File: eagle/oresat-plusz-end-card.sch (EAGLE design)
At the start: 13 parts, among them J1 J-SAMTEC-TFM-110-X1-XXX-D-RA, J2 U.FL

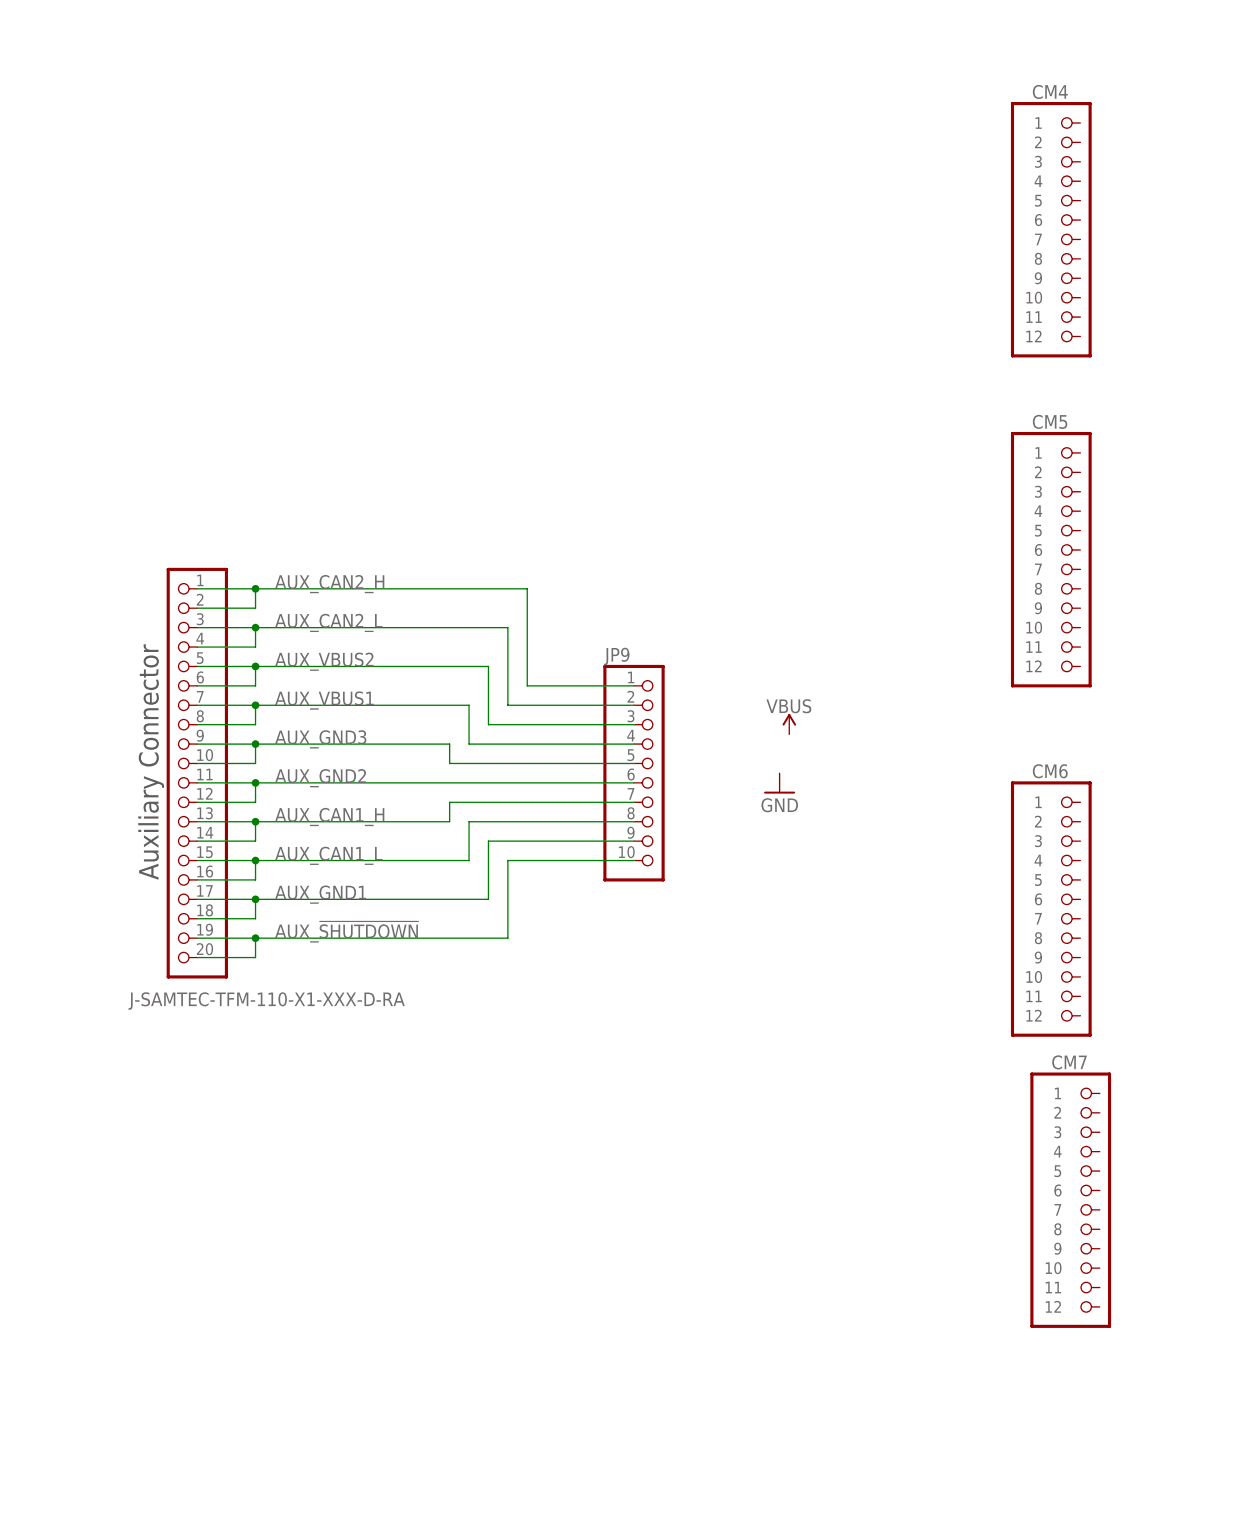
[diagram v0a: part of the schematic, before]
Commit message: Created library and placed solar connectors based on structure updates from yesterday.
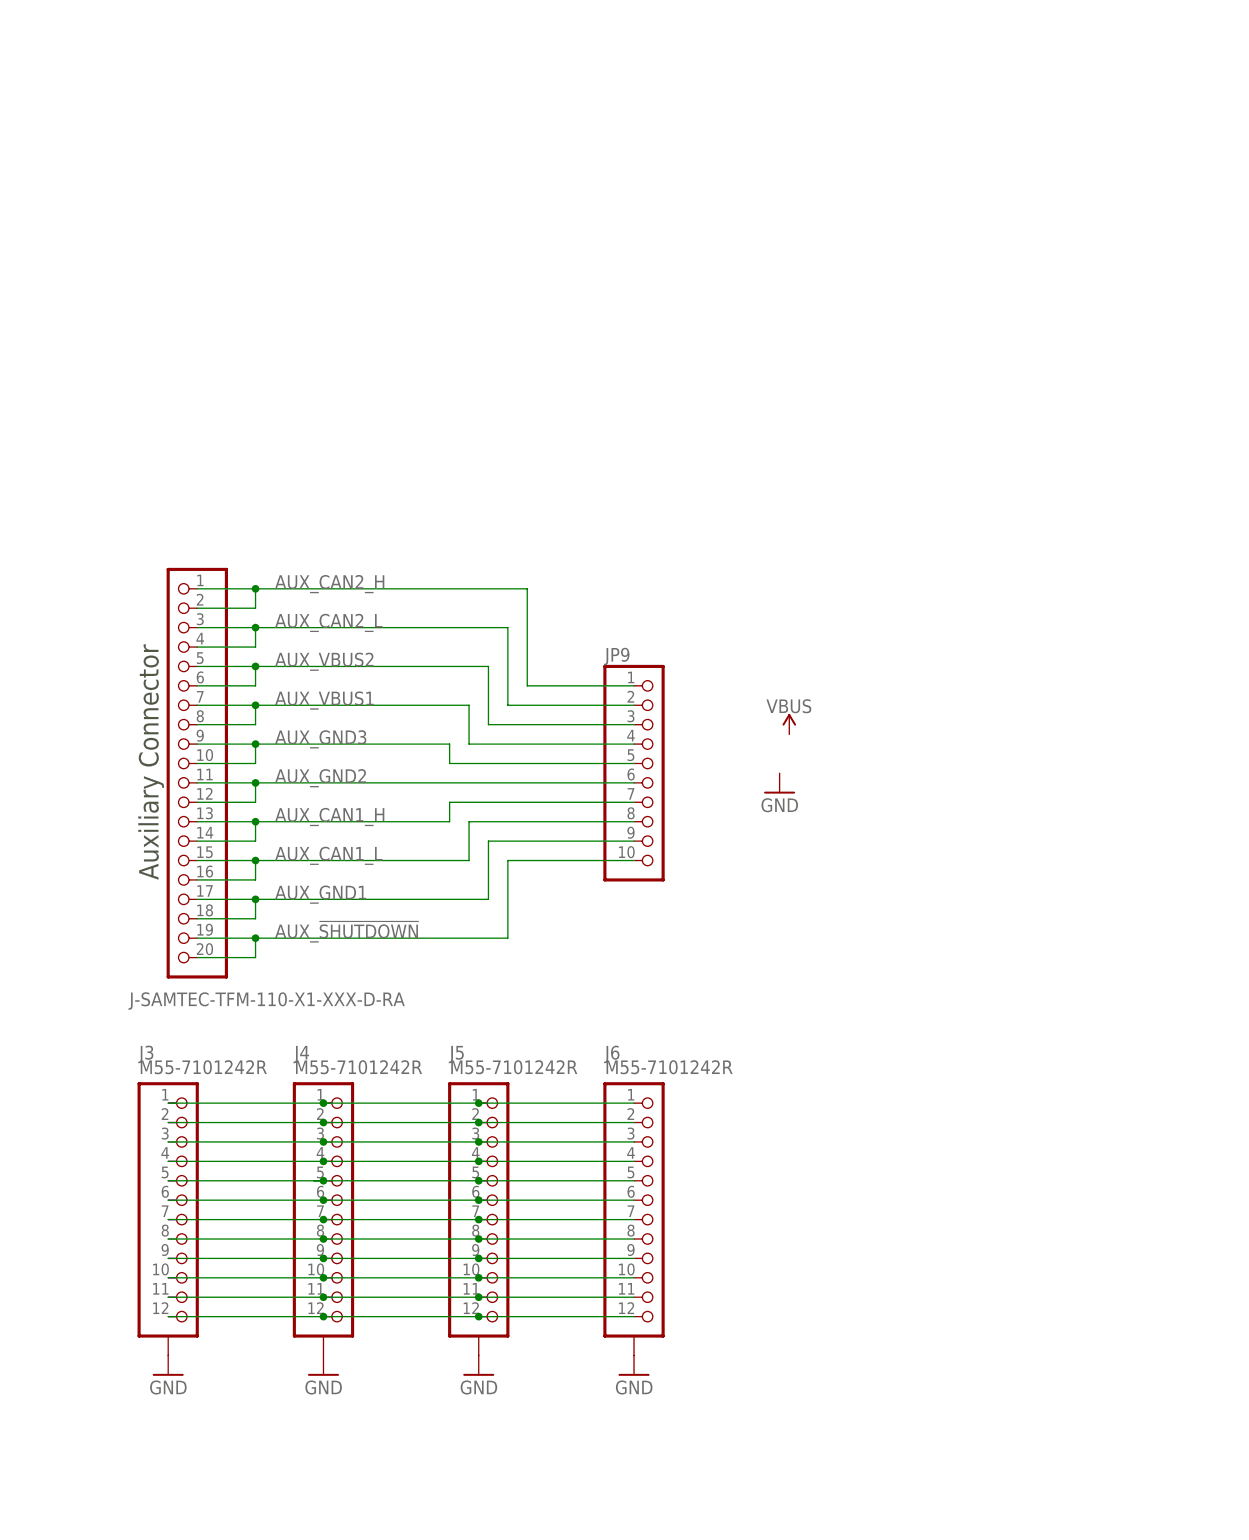
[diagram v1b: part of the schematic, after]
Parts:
- removed CM4, CM5, CM6, CM7: ORESAT-SOLARPANEL-CARD-12PIN, oresat-connectors:ORESAT-SOLARPANEL-CARD-12PIN
- added J3, J4, J5, J6: M55-7101242R, J-Harwin-M55-7101242:M55-7101242R
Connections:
- new net N$1: J3.1, J4.1, J5.1, J6.1
- new net N$10: J3.10, J4.10, J5.10, J6.10
- new net N$11: J3.11, J4.11, J5.11, J6.11
- new net N$12: J3.12, J4.12, J5.12, J6.12
- new net N$2: J3.2, J4.2, J5.2, J6.2
- new net N$3: J3.3, J4.3, J5.3, J6.3
- new net N$4: J3.4, J4.4, J5.4, J6.4
- new net N$5: J3.5, J4.5, J5.5, J6.5
- new net N$6: J3.6, J4.6, J5.6, J6.6
- new net N$7: J3.7, J4.7, J5.7, J6.7
- new net N$8: J3.8, J4.8, J5.8, J6.8
- new net N$9: J3.9, J4.9, J5.9, J6.9
- net GND: now also J3.SHIELD, J4.SHIELD, J5.SHIELD, J6.SHIELD

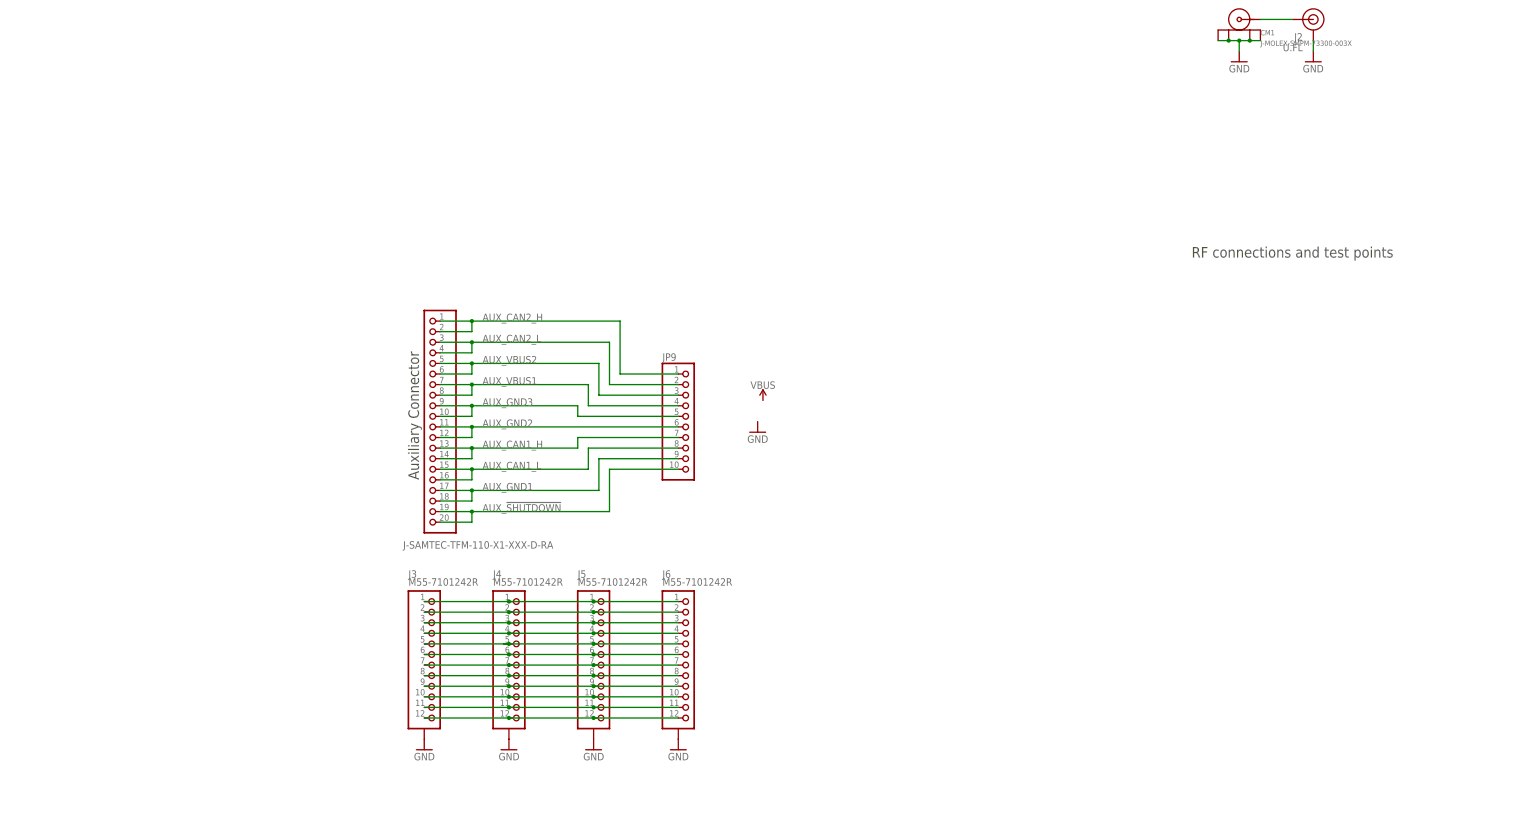
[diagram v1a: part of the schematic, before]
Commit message: Worked with Joe to check connectors, preliminary layout, 2 layers for now.
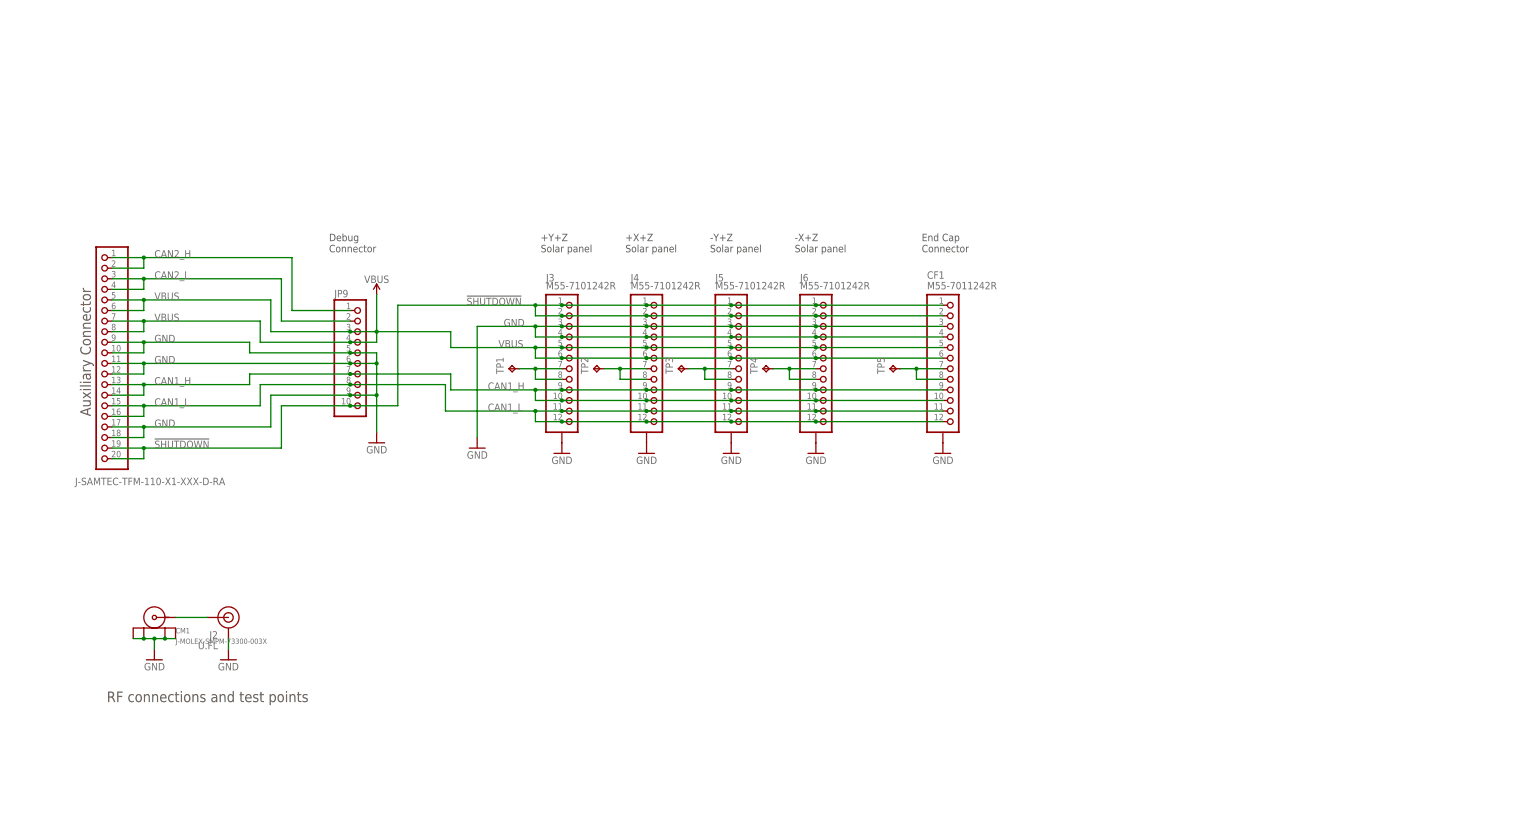
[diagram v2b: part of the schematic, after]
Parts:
- added CF1: M55-7011242R, J-Harwin-M55-6021242R:J-HARWIN-M55-6021242R
- added TP1, TP2, TP3, TP4, TP5: TPPAD1-13, testpad:TPPAD1-13
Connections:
- net AUX_CAN2_H renamed CAN2_H
- net AUX_CAN2_L renamed CAN2_L
- removed net AUX_!SHUTDOWN: J1.19, J1.20, JP9.10
- removed net AUX_CAN1_H: J1.13, J1.14, JP9.7
- removed net AUX_CAN1_L: J1.15, J1.16, JP9.8
- removed net AUX_GND1: J1.17, J1.18, JP9.9
- removed net AUX_GND2: J1.11, J1.12, JP9.6
- removed net AUX_GND3: J1.10, J1.9, JP9.5
- removed net AUX_VBUS1: J1.7, J1.8, JP9.4
- removed net AUX_VBUS2: J1.5, J1.6, JP9.3
- removed net N$10: J3.10, J4.10, J5.10, J6.10
- removed net N$11: J3.11, J4.11, J5.11, J6.11
- removed net N$12: J3.12, J4.12, J5.12, J6.12
- removed net N$6: J3.6, J4.6, J5.6, J6.6
- removed net N$7: J3.7, J4.7, J5.7, J6.7
- removed net N$8: J3.8, J4.8, J5.8, J6.8
- removed net N$9: J3.9, J4.9, J5.9, J6.9
- new net !SHUTDOWN: CF1.1, CF1.2, J1.19, J1.20, J3.1, J3.2, J4.1, J4.2, J5.1, J5.2, J6.1, J6.2, JP9.10
- new net CAN1_H: CF1.10, CF1.9, J1.13, J1.14, J3.10, J3.9, J4.10, J4.9, J5.10, J5.9, J6.10, J6.9, JP9.7
- new net CAN1_L: CF1.11, CF1.12, J1.15, J1.16, J3.11, J3.12, J4.11, J4.12, J5.11, J5.12, J6.11, J6.12, JP9.8
- new net VBUS: CF1.5, CF1.6, J1.5, J1.6, J1.7, J1.8, J3.5, J3.6, J4.5, J4.6, J5.5, J5.6, J6.5, J6.6, JP9.3, JP9.4
- net GND: now also CF1.3, CF1.4, CF1.SHIELDS, J1.10, J1.11, J1.12, J1.17, J1.18, J1.9, J3.3, J3.4, J4.3, J4.4, J5.3, J5.4, J6.3, J6.4, JP9.5, JP9.6, JP9.9
- net N$1: now also J4.7, J4.8, TP2.TP; no longer J3.1, J4.1, J5.1, J6.1
- net N$2: now also J3.7, J3.8, TP1.TP; no longer J3.2, J4.2, J5.2, J6.2
- net N$3: now also CF1.7, CF1.8, TP5.TP; no longer J3.3, J4.3, J5.3, J6.3
- net N$4: now also J5.7, J5.8, TP3.TP; no longer J3.4, J4.4, J5.4, J6.4
- net N$5: now also J6.7, J6.8, TP4.TP; no longer J3.5, J4.5, J5.5, J6.5
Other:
- note added: "+X+Z Solar panel"
- note added: "+Y+Z Solar panel"
- note added: "-X+Z Solar panel"
- note added: "-Y+Z Solar panel"
- note added: "Debug Connector"
- note added: "End Cap Connector"
- moved on the sheet: CM1, J2, J3, J4, J5, J6, JP9

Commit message: Updated +Z end card, with end cap attachment to magnetometers.
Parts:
- removed TP5: TPPAD1-13, testpad:TPPAD1-13
- added C1: 10u, oresat-rcl:C-EU0603-B-NOSILK
- added C10, C11: 22u, oresat-rcl:C-EU0805-B-NOSILK
- added C12, C15, C18, C2, C8: 100n, rcl_custom:C-EU0402-B-NOSILK
- added C13, C14: 20p, rcl_custom:C-EU0402-B-NOSILK
- added C3, C7: 10u, oresat-rcl:C-EU0805-B-NOSILK
- added C9: 22u, oresat-rcl:C-EU0603-B-NOSILK
- added D1: GREEN, SparkFun-LED:LED-GREEN0603
- added J8: FTSH-105-XX-X-DV-K, J-Samtec-FTSH-105-XXX-DV-K-ARM-SWD:FTSH-105-XX-X-DV-K
- added L1: 1.5 uH, L-Coilcraft-XFL4020:L-COILCRAFT-XFL4020
- added R1, R11, R4, R8: 10k, rcl_custom:R-US_0402-B-NOSILK
- added R10, R7: 4.7k, rcl_custom:R-US_0402-B-NOSILK
- added R2: 470k, rcl_custom:R-US_0402-B-NOSILK
- added R3: 150k, rcl_custom:R-US_0402-B-NOSILK
- added R5, R6: NP, rcl_custom:R-US_0402-B-NOSILK
- added R9: 2.7k, rcl_custom:R-US_0402-B-NOSILK
- added TP11, TP12, TP13, TP14, TP15, TP7: TEST-POINT, Tova:TEST-POINT
- added U2: TPS63070, ic-pwr-tps63070x:TPS63070X
- added U3: TCAN330, TCAN330:TCAN330
- added U4: STM32F042K6, STM32F042K:STM32F042K6
- added X2: 16MHZ-2.5x2mm, low-gain-radio:CRYSTAL-WITH-GND
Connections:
- removed net N$3: CF1.7, CF1.8, TP5.TP
- new net 3.3V: C10.1, C11.1, C12.2, C15.2, C18.2, C8.2, C9.1, CF1.11, CF1.12, J8.VTREF, R10.2, R11.2, R2.2, R5.2, R7.2, TP11.1, U2.VOUT, U3.VCC, U4.VDD, U4.VDDA, U4.VDDIO2
- new net BOOT1: R8.2, TP7.1, U4.PB8-BOOT0
- new net CAN_RX: U3.RXD, U4.PA11
- new net CAN_SHDN: U3.SHDN, U4.PA10
- new net CAN_SILENT: U3.S, U4.PA9
- new net CAN_TX: U3.TXD, U4.PA12
- new net CRYSTALIN1: C14.1, U4.PF0-OSC_IN, X2.1
- new net CRYSTALOUT1: C13.1, U4.PF1-OSC_OUT, X2.2
- new net N$7: D1.A, R9.1
- new net NRESET: J8.!RESET, U4.NRST
- new net PA0: R9.2, U4.PA0
- new net PA1: U4.PA1
- new net PA15: U4.PA15
- new net PA2/USART2_TX: U4.PA2
- new net PA3/USART2_RX: U4.PA3
- new net PA4: U4.PA4
- new net PA5/SPI1_SCK: U4.PA5
- new net PA6/SPI1_MISO: U4.PA6
- new net PA7/SPI1_MOSI: U4.PA7
- new net PA8: U4.PA8
- new net PB0: U4.PB0
- new net PB1: U4.PB1
- new net PB3: U4.PB3
- new net PB4/I2C-!RESET: CF1.3, CF1.4, U4.PB4
- new net PB5/I2C-!INT: CF1.5, CF1.6, R11.1, U4.PB5
- new net PB6/SCL: CF1.7, CF1.8, R7.1, U4.PB6
- new net PB7/SDA: CF1.10, CF1.9, R10.1, U4.PB7
- new net SWCLK: J8.SWDCLK/TCK, U4.PA14-SWCLK
- new net SWDIO: J8.SWDIO/TMS, U4.PA13-SWDIO
- new net TPS-EN2: R1.1, R6.2, TP15.1, U2.EN, U2.PS/SYNC
- new net TPS-FB2: R2.1, R3.2, U2.FB
- new net TPS-FB4: TP13.1, U2.FB2
- new net TPS-L1: L1.1, U2.L1
- new net TPS-L2: L1.2, U2.L2
- new net TPS-PG2: R5.1, TP12.1, U2.PG
- new net TPS-VAUX2: C2.1, U2.VAUX
- new net TPS-VSEL2: R4.2, TP14.1, U2.VSEL
- net !SHUTDOWN: no longer CF1.1, CF1.2
- net CAN1_H: now also U3.CANH; no longer CF1.10, CF1.9
- net CAN1_L: now also U3.CANL; no longer CF1.11, CF1.12
- net GND: now also C1.2, C10.2, C11.2, C12.1, C13.2, C14.2, C15.1, C18.1, C2.2, C3.2, C7.2, C8.1, C9.2, CF1.1, CF1.2, D1.C, J8.GND, J8.GND@2, J8.GNDDET, R3.1, R4.1, R6.1, R8.1, U2.GND, U2.PGND, U3.GND, U4.VSS, X2.SHIELD; no longer CF1.3, CF1.4
- net VBUS: now also C1.1, C3.1, C7.1, R1.2, U2.VIN; no longer CF1.5, CF1.6
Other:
- note added: "!RESET to the TCA should be pulled high by the STM"
- note added: "0603"
- note added: "0805"
- note added: "10 pn 1.27mm ARM SWD connector"
- note added: "CAN Transceiver"
- note added: "NRST pull-up built in"
- moved on the sheet: CF1, CM1, J2, J3, J4, J5, J6, JP9, TP1, TP2, TP3, TP4

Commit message: Updated end cards with antenna keep outs, and rewired +Z end card debug port and started on +Z schematic update with power domain.
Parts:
- removed H3: STAND-OFFTIGHT, SparkFun-Hardware:STAND-OFFTIGHT
- removed J1: J-SAMTEC-TFM-110-X1-XXX-D-RA, J-Samtec-TFM-110-X1-XXX-D-RA:J-SAMTEC-TFM-110-X1-XXX-D-RA
- removed JP9: (no value), pinhead:PINHD-1X10
- added CF2: J-HARWIN-M55-70X1242R, J-Harwin-M55-70X1242R-12pin-1.27mm-M-vertical:J-HARWIN-M55-70X1242R
- added J7: J-SAMTEC-TFM-120-X1-XXX-D-RA, J-Samtec-TFM-120-X1-XXX-D-RA:J-SAMTEC-TFM-120-X1-XXX-D-RA
- CF1: value M55-7011242R -> J-HARWIN-M55-70X1242R; device J-Harwin-M55-6021242R:J-HARWIN-M55-6021242R -> J-Harwin-M55-70X1242R-12pin-1.27mm-M-vertical:J-HARWIN-M55-70X1242R
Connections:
- new net N$15: J7.13, J7.14
- new net OPD_PWR: CF1.12, J7.19, J7.20
- new net OPD_SCL: CF1.9, J7.17, J7.18
- new net OPD_SDA: CF1.11, J7.15, J7.16
- new net SPARE1: J7.11, J7.12
- new net SPARE2: J7.10, J7.9
- new net SPARE3: J7.7, J7.8
- new net SPARE4: J7.5, J7.6
- new net SPARE5: J7.3, J7.4
- new net SPARE6: J7.1, J7.2
- net !SHUTDOWN: now also CF1.10, J7.39, J7.40; no longer J1.19, J1.20, JP9.10
- net 3.3V: now also CF2.1, CF2.2; no longer CF1.11, CF1.12
- net CAN1_H: now also CF1.1, J7.33, J7.34; no longer J1.13, J1.14, JP9.7
- net CAN1_L: now also CF1.2, J7.35, J7.36; no longer J1.15, J1.16, JP9.8
- net CAN2_H: now also CF1.7, J7.21, J7.22; no longer J1.1, J1.2, JP9.1
- net CAN2_L: now also CF1.8, J7.23, J7.24; no longer J1.3, J1.4, JP9.2
- net GND: now also CF1.3, CF1.4, CF2.11, CF2.12, CF2.SHIELDS, J7.29, J7.30, J7.31, J7.32, J7.37, J7.38; no longer CF1.1, CF1.2, J1.10, J1.11, J1.12, J1.17, J1.18, J1.9, JP9.5, JP9.6, JP9.9
- net PB4/I2C-!RESET: now also CF2.10, CF2.9; no longer CF1.3, CF1.4
- net PB5/I2C-!INT: now also CF2.7, CF2.8; no longer CF1.5, CF1.6
- net PB6/SCL: now also CF2.5, CF2.6; no longer CF1.7, CF1.8
- net PB7/SDA: now also CF2.3, CF2.4; no longer CF1.10, CF1.9
- net VBUS: now also CF1.5, CF1.6, J7.25, J7.26, J7.27, J7.28; no longer J1.5, J1.6, J1.7, J1.8, JP9.3, JP9.4
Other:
- note added: "+Z End Cap Connector (+Z Magnetometers)"
- note added: "Main Backplane Connector"
- note added: "OreSat Debug"
- note removed: "Auxiliary Connector"
- note removed: "Debug Connector"
- note removed: "End Cap Connector"
